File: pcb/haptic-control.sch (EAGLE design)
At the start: 47 parts, among them M1 SPH0641LM4H-1, U1 CC2642R, U2 SST26VF064B, U3 ICM20948, U4 74LVC1G17, U5 MCP1700T-1802TT, U6 PCA9306-DCU, U7 MTCH6301, X1 48MHz, X2 32.768kHz

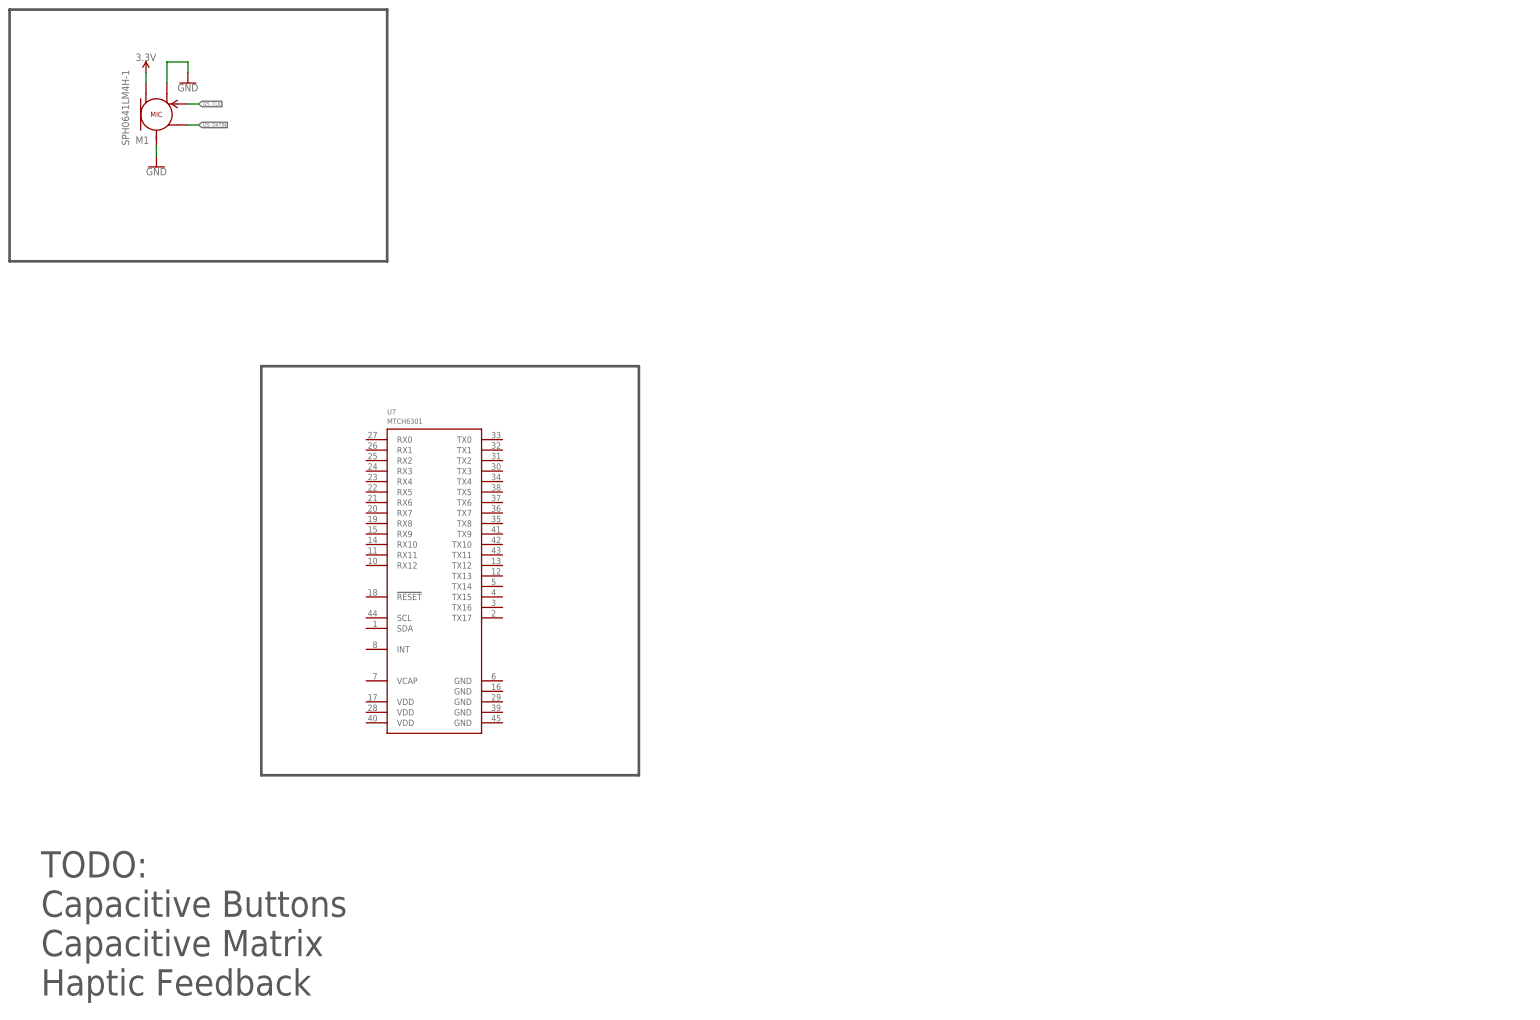
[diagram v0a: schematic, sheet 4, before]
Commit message: minor sch value modifications, and ic additions; minor pcb constraints changes
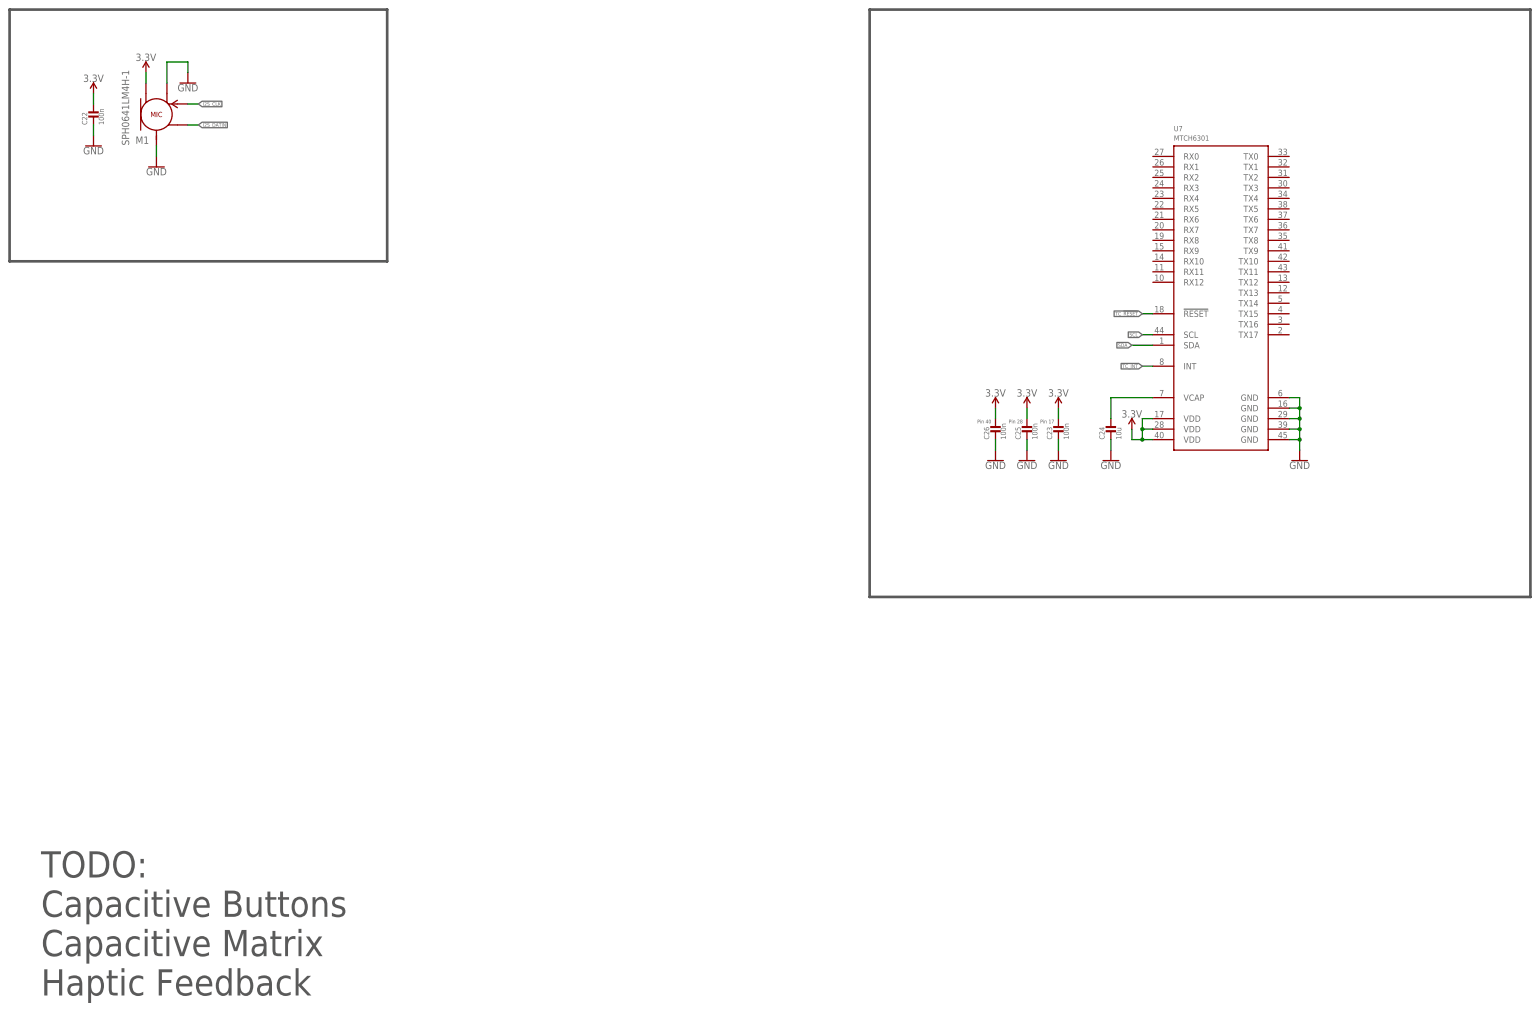
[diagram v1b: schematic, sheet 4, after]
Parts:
- added A1: U.FL, Connectors > Antennas:U.FL
- added C22, C23, C25, C26: 100n, Passive Components > Capacitors > Multilayer Ceramic Capacitors MLCC:MLCC_0402
- added C24: 10u, Passive Components > Capacitors > Multilayer Ceramic Capacitors MLCC:MLCC0603
- added C27: 100u, Passive Components > Capacitors > Multilayer Ceramic Capacitors MLCC:MLCC_1206
- added TP4, TP5: TEST_POINT, Utility > Board:TEST_POINT
- added U$1: FS312F-G, Power > Battery Management:FS312F-G
- added U$2: FS8205, Semiconductors > Discrete Semiconductors > Transistors > MOSFETs:FS8205
- added U8: BQ51050B, Texas Instruments:BQ51050B
- C10, C9: value 3p -> 12p
- C11, C12: value (none) -> np
- C4: value (none) -> 22u
- C6: value 10u -> 22u
- L1: value 10u -> 6u8
- L2: value filter -> BLM18HE152SN1
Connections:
- new net N$10: C24.P$1, U7.VCAP
- new net TC_!RESET: U7.!RESET
- new net TC_INT: U7.INT
- net 3.3V: now also C22.P$1, C23.P$1, C25.P$1, C26.P$1, C27.P$1, U7.VDD@0, U7.VDD@1, U7.VDD@2
- net GND: now also C22.P$2, C23.P$2, C24.P$2, C25.P$2, C26.P$2, C27.P$2, U7.GND@0, U7.GND@1, U7.GND@2, U7.GND@3, U7.GND@4
- net SCL: now also U7.SCL
- net SDA: now also U7.SDA
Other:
- note added: "Pin 17"
- note added: "Pin 28"
- note added: "Pin 40"
- moved on the sheet: C1, C2, C3, C4, C5, L2, U7

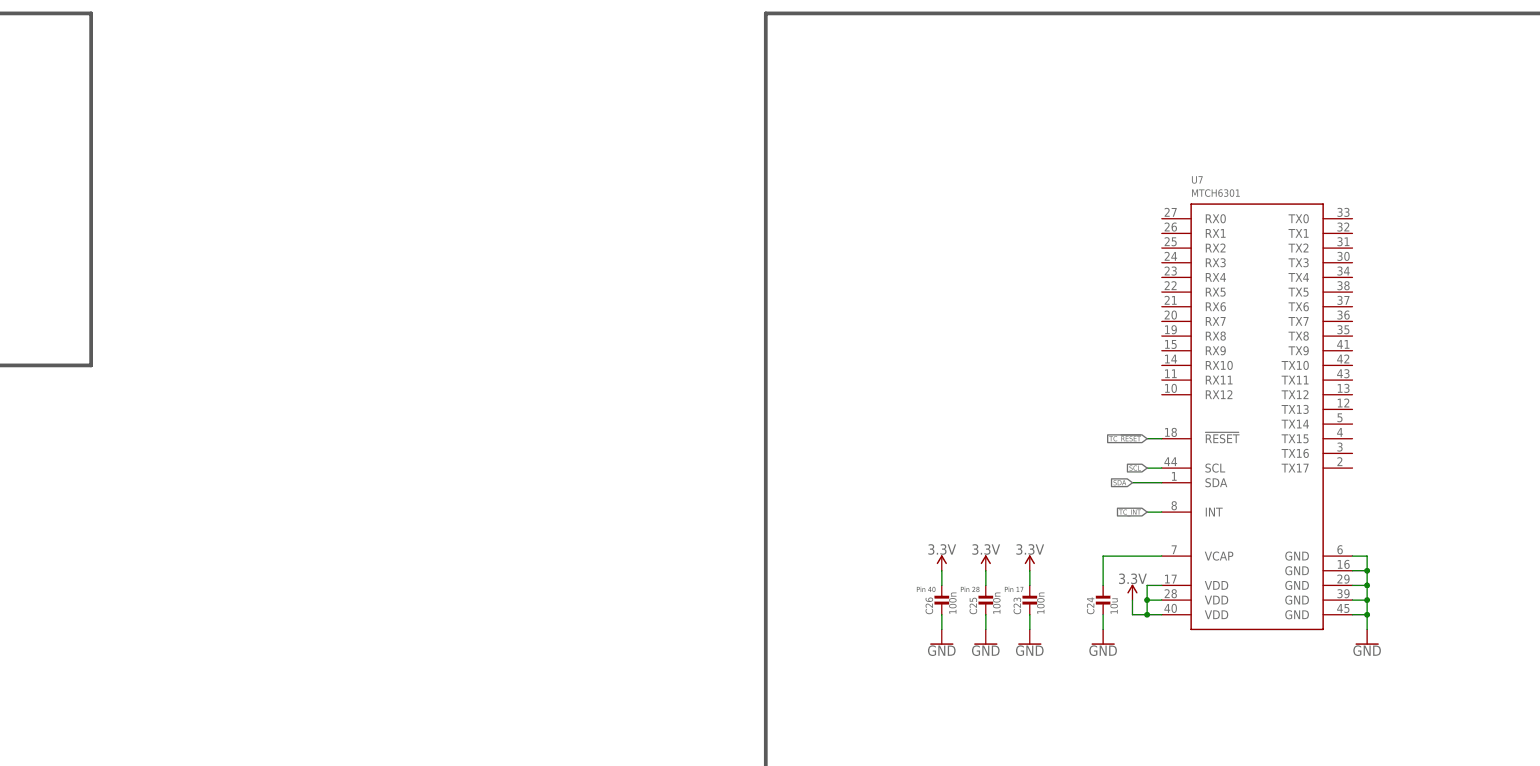
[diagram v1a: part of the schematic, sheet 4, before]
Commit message: Hand merged previous commits: 	Added CC26x2 reference design 	Added antenna matching 	Connected labels to touch IC 	Added keepouts for the antenna 	Added more references/info to the board and schematic
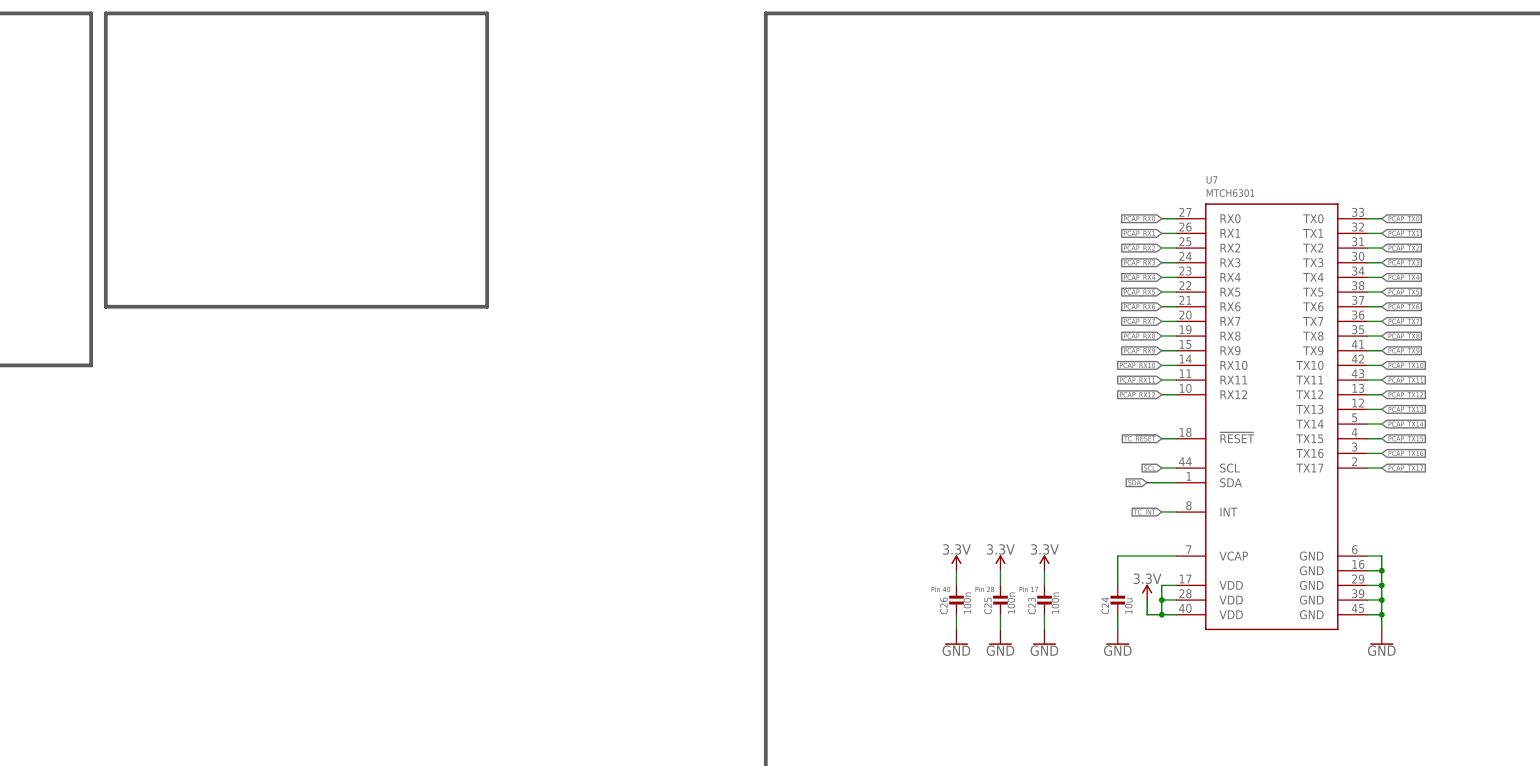
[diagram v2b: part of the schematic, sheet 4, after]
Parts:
- removed TP4, TP5: TEST_POINT, Utility > Board:TEST_POINT
- added C28, C29, C31: 1p, Passive Components > Capacitors > Multilayer Ceramic Capacitors MLCC:MLCC_0402
- added C30, C33: 12p, Passive Components > Capacitors > Multilayer Ceramic Capacitors MLCC:MLCC_0402
- added C32: 1p8, Passive Components > Capacitors > Multilayer Ceramic Capacitors MLCC:MLCC_0402
- added C34, C35: DNP, Passive Components > Capacitors > Multilayer Ceramic Capacitors MLCC:MLCC_0402
- added L3, L4: 2n4, Passive Components > Inductors, Chokes & Coils:INDUCTOR_NC_0402
- added L5, L6: 2N, Passive Components > Inductors, Chokes & Coils:INDUCTOR_NC_0402
- added P1, P2: 2P-PAD, Generic Connector:2P-PAD
- C11, C12: value np -> DNP
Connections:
- new net N$14: C30.P$1, L3.P$1
- new net N$15: C29.P$1, L4.P$1, L5.P$2
- new net N$16: C31.P$1, L5.P$1, L6.P$2
- new net N$17: C32.P$2, C35.P$1, E1.SIGNAL
- new net N$18: C32.P$1, C33.P$2
- new net N$19: C33.P$1, C34.P$2, L6.P$1
- new net N$20: A1.SIGNAL, C34.P$1
- new net PCAP_RX0: U7.RX0
- new net PCAP_RX1: U7.RX1
- new net PCAP_RX10: U7.RX10
- new net PCAP_RX11: U7.RX11
- new net PCAP_RX12: U7.RX12
- new net PCAP_RX2: U7.RX2
- new net PCAP_RX3: U7.RX3
- new net PCAP_RX4: U7.RX4
- new net PCAP_RX5: U7.RX5
- new net PCAP_RX6: U7.RX6
- new net PCAP_RX7: U7.RX7
- new net PCAP_RX8: U7.RX8
- new net PCAP_RX9: U7.RX9
- new net PCAP_TX0: U7.TX0
- new net PCAP_TX1: U7.TX1
- new net PCAP_TX10: U7.TX10
- new net PCAP_TX11: U7.TX11
- new net PCAP_TX12: U7.TX12
- new net PCAP_TX13: U7.TX13
- new net PCAP_TX14: U7.TX14
- new net PCAP_TX15: U7.TX15
- new net PCAP_TX16: U7.TX16
- new net PCAP_TX17: U7.TX17
- new net PCAP_TX2: U7.TX2
- new net PCAP_TX3: U7.TX3
- new net PCAP_TX4: U7.TX4
- new net PCAP_TX5: U7.TX5
- new net PCAP_TX6: U7.TX6
- new net PCAP_TX7: U7.TX7
- new net PCAP_TX8: U7.TX8
- new net PCAP_TX9: U7.TX9
- net GND: now also A1.GND@0, A1.GND@1, C28.P$1, C30.P$2, C31.P$2, C35.P$2, E1.GND
- net N$1: now also C28.P$2, L4.P$2
- net N$3: now also C29.P$2, L3.P$2
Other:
- note added: "Mount either C33 or C34"
- note added: "SDO LOW: I2C Address: 0xD0"
- note removed: "TODO: Antenna matching"
- moved on the sheet: C23, C24, C25, C26, E1, U7

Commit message: added battery and coil pads, changed mcu orientation
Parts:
- removed P1, P2: 2P-PAD, Generic Connector:2P-PAD
- removed U$1: FS312F-G, Power > Battery Management:FS312F-G
- removed U$2: FS8205, Semiconductors > Discrete Semiconductors > Transistors > MOSFETs:FS8205
- added J1, J2: PAD1X3_5MM-2P, Connectors > Other:PAD1X3_5MM-2P
- added U10: FS8205, Fortune:FS8205
- added U9: FS312F-G, Fortune:FS312F-G
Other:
- note added: "TODO: Capacitive Buttons Capacitive Matrix Haptic Feedback LRA"
- note removed: "TODO: Capacitive Buttons Capacitive Matrix Haptic Feedback"
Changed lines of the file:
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@@
 <?xml version="1.0" encoding="utf-8"?>
 <!DOCTYPE eagle SYSTEM "eagle.dtd">
-<eagle version="9.3.0">
+<eagle version="9.3.2">
 <drawing>
 <settings>
@@
 <part name="A1" library="Connectors &gt; Antennas" deviceset="U.FL" device=""/>
 <part name="U8" library="Texas Instruments" deviceset="BQ51050B" device=""/>
-<part name="U$1" library="Power &gt; Battery Management" deviceset="FS312F-G" device=""/>
-<part name="U$2" library="Semiconductors &gt; Discrete Semiconductors &gt; Transistors &gt; MOSFETs" deviceset="FS8205" device=""/>
 <part name="C28" library="Passive Components &gt; Capacitors &gt; Multilayer Ceramic Capacitors MLCC" deviceset="MLCC" device="_0402" value="1p"/>
 <part name="C29" library="Passive Components &gt; Capacitors &gt; Multilayer Ceramic Capacitors MLCC" deviceset="MLCC" device="_0402" value="1p"/>
@@
 <part name="C33" library="Passive Components &gt; Capacitors &gt; Multilayer Ceramic Capacitors MLCC" deviceset="MLCC" device="_0402" value="12p"/>
 <part name="C32" library="Passive Components &gt; Capacitors &gt; Multilayer Ceramic Capacitors MLCC" deviceset="MLCC" device="_0402" value="1p8"/>
-<part name="P1" library="Generic Connector" deviceset="2P-PAD" device=""/>
-<part name="P2" library="Generic Connector" deviceset="2P-PAD" device=""/>
+<part name="U9" library="Fortune" deviceset="FS312F-G" device=""/>
+<part name="U10" library="Fortune" deviceset="FS8205" device=""/>
+<part name="J1" library="Connectors &gt; Other" deviceset="PAD1X3_5MM-2P" device=""/>
+<part name="J2" library="Connectors &gt; Other" deviceset="PAD1X3_5MM-2P" device=""/>
 </parts>
 <sheets>
@@
 <attribute name="VALUE" x="223.52" y="214.63" size="1.27" layer="96"/>
 </instance>
-<instance part="U$1" gate="G$1" x="279.4" y="193.04" smashed="yes"/>
-<instance part="U$2" gate="G$1" x="309.88" y="193.04" smashed="yes"/>
-<instance part="P1" gate="-1" x="208.28" y="200.66" smashed="yes">
-<attribute name="NAME" x="210.82" y="199.898" size="1.524" layer="95"/>
-<attribute name="VALUE" x="207.518" y="202.057" size="1.524" layer="96"/>
-</instance>
-<instance part="P1" gate="-2" x="208.28" y="198.12" smashed="yes">
-<attribute name="NAME" x="210.82" y="197.358" size="1.524" layer="95"/>
-</instance>
-<instance part="P2" gate="-1" x="309.88" y="205.74" smashed="yes">
-<attribute name="NAME" x="312.42" y="204.978" size="1.524" layer="95"/>
-<attribute name="VALUE" x="309.118" y="207.137" size="1.524" layer="96"/>
-</instance>
-<instance part="P2" gate="-2" x="309.88" y="203.2" smashed="yes">
-<attribute name="NAME" x="312.42" y="202.438" size="1.524" layer="95"/>
+<instance part="U9" gate="G$1" x="287.02" y="198.12" smashed="yes">
+<attribute name="NAME" x="271.78" y="200.66" size="1.27" layer="95"/>
+<attribute name="VALUE" x="271.78" y="198.882" size="1.27" layer="96"/>
+</instance>
+<instance part="U10" gate="G$1" x="322.58" y="198.12" smashed="yes">
+<attribute name="NAME" x="324.612" y="196.596" size="1.27" layer="95"/>
+<attribute name="VALUE" x="324.612" y="194.31" size="1.27" layer="96"/>
+</instance>
+<instance part="J1" gate=".1" x="203.2" y="195.58" smashed="yes">
+<attribute name="NAME" x="205.74" y="194.818" size="1.524" layer="95"/>
+</instance>
+<instance part="J1" gate=".2" x="203.2" y="193.04" smashed="yes">
+<attribute name="NAME" x="205.74" y="192.278" size="1.524" layer="95"/>
+</instance>
+<instance part="J2" gate=".1" x="287.02" y="208.28" smashed="yes">
+<attribute name="NAME" x="289.56" y="207.518" size="1.524" layer="95"/>
+</instance>
+<instance part="J2" gate=".2" x="287.02" y="205.74" smashed="yes">
+<attribute name="NAME" x="289.56" y="204.978" size="1.524" layer="95"/>
 </instance>
 </instances>
@@
 Capacitive Buttons
 Capacitive Matrix
-Haptic Feedback</text>
+Haptic Feedback
+LRA</text>
 <wire x1="5.08" y1="246.38" x2="96.52" y2="246.38" width="0.645159375" layer="97"/>
 <wire x1="96.52" y1="246.38" x2="96.52" y2="185.42" width="0.645159375" layer="97"/>
